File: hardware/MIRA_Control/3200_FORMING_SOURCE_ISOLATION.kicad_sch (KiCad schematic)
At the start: 11 parts, among them U3200 ADG5412BFBRUZ

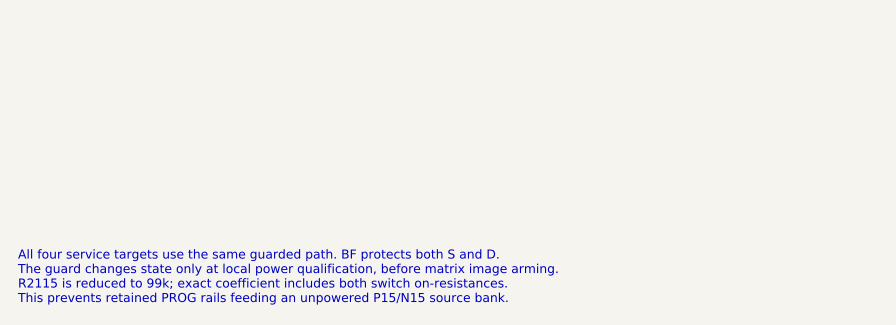
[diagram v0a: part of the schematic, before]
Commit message: MIRA.05: analog requirements and schematic fixes
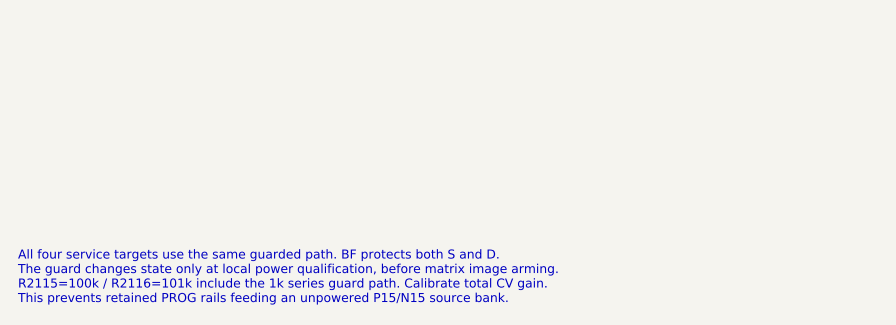
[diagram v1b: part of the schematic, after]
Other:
- note added: "All four service targets use the same guarded path. BF protects both S and D. The guard changes state only at local power qualification, before matrix image arming. R2115=100k / R2116=101k include the 1k series guard path. Calibrate total CV gain. This prevents retained PROG rails feeding an unpowered P15/N15 source bank."
- note removed: "All four service targets use the same guarded path. BF protects both S and D. The guard changes state only at local power qualification, before matrix image arming. R2115 is reduced to 99k; exact coefficient includes both switch on-resistances. This prevents retained PROG rails feeding an unpowered P15/N15 source bank."
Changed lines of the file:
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@@
 (global_label "GND" (shape input) (at 347.98 238.76 0) (effects (font (size 0.8 0.8)) (justify left)))
 (symbol (lib_id "MIRA_RevA:SIG_C_100n") (at 332.74 238.76 0) (unit 1) (in_bom yes) (on_board yes) (dnp no) (property "Reference" "C3201" (at 332.74 231.14 0) (show_name no) (do_not_autoplace no) (effects (font (size 1 1)))) (property "Value" "100n" (at 332.74 233.67999999999998 0) (show_name no) (do_not_autoplace no) (effects (font (size 1 1)))) (property "Footprint" "MIRA_RevA:C_0402_1005Metric" (at 332.74 233.67999999999998 0) (show_name no) (do_not_autoplace no) (hide yes) (effects (font (size 1 1))) (hide yes)) (property "Datasheet" "" (at 332.74 233.67999999999998 0) (show_name no) (do_not_autoplace no) (hide yes) (effects (font (size 1 1))) (hide yes)) (property "Description" "MLCC, 100nF, 16V, X7R, 0402" (at 332.74 233.67999999999998 0) (show_name no) (do_not_autoplace no) (hide yes) (effects (font (size 1 1))) (hide yes)) (property "MPN" "GRM155R71H104KE14D" (at 332.74 233.67999999999998 0) (show_name no) (do_not_autoplace no) (hide yes) (effects (font (size 1 1))) (hide yes)) (property "Manufacturer" "Murata" (at 332.74 233.67999999999998 0) (show_name no) (do_not_autoplace no) (hide yes) (effects (font (size 1 1))) (hide yes)) (pin "1") (pin "2") (instances (project "MIRA_Control" (path "/ad010b50-c509-466c-b833-d1667dfb0702/fd0f6d5b-bd8a-4d0f-aeb4-8f4774567883" (reference "C3201") (unit 1)))))
-(text "All four service targets use the same guarded path. BF protects both S and D.\nThe guard changes state only at local power qualification, before matrix image arming.\nR2115 is reduced to 99k; exact coefficient includes both switch on-resistances.\nThis prevents retained PROG rails feeding an unpowered P15/N15 source bank." (at 15.24 262.89 0) (effects (font (size 1 1)) (justify left top)))
+(text "All four service targets use the same guarded path. BF protects both S and D.\nThe guard changes state only at local power qualification, before matrix image arming.\nR2115=100k / R2116=101k include the 1k series guard path. Calibrate total CV gain.\nThis prevents retained PROG rails feeding an unpowered P15/N15 source bank." (at 15.24 262.89 0) (effects (font (size 1 1)) (justify left top)))
 (embedded_fonts no)
 )
